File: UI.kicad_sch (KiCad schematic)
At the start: 15 parts, among them J501 EXT LEDS, SW501 SW_Push, SW502 SW_Push

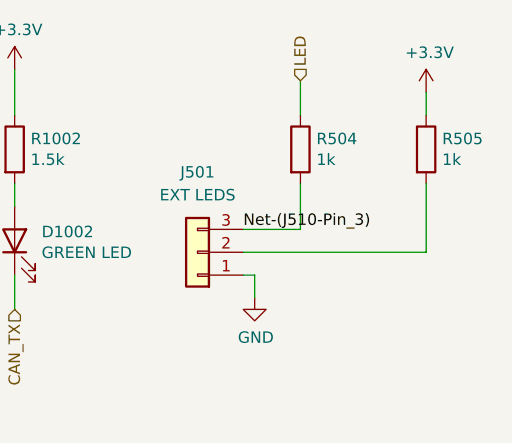
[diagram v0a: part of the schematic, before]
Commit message: Adjust external LED resistor values for ~5 mA drive current
Added series resistors for optional external panel LEDs on the GPIO13 (blue)
and 3V3 (red) indicator lines. On-board LEDs retain their existing 2 kΩ
resistors; external LEDs now use separate resistors sized for ~5 mA.

Red LED:
- Vf ≈ 2.1 V
- Vr = 3.3 V – 2.1 V = 1.2 V
- R = 1.2 V / 0.005 A = 240 Ω

Blue LED:
- Vf typically ≈ 3.0 V at a few mA (3.3 V worst case simply reduces brightness)
- Vr = 3.3 V – 3.0 V = 0.3 V
- R = 0.3 V / 0.005 A = 75 Ω

Resulting currents fall in the 3–5 mA range depending on LED tolerance, with
total GPIO13 load remaining well below ESP32-S3 limits. Red and blue LEDs now
have comparable perceived brightness.

Resistor values added:
- External red LED: 240 Ω
- External blue LED: 75 Ω
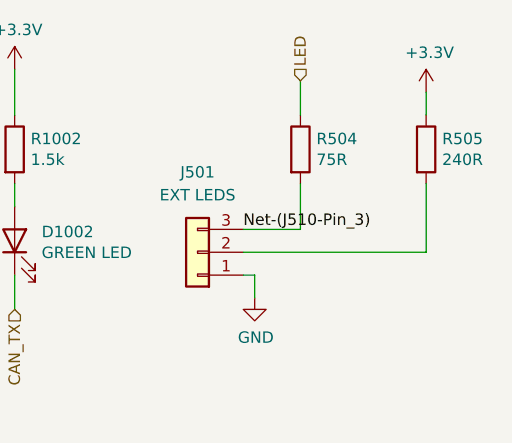
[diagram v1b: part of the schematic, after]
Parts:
- R504: value 1k -> 75R; LCSC C11702 -> C25133
- R505: value 1k -> 240R; LCSC C11702 -> C25094
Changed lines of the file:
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@@
 			)
 		)
-		(property "Value" "1k"
+		(property "Value" "75R"
 			(at 127.508 37.973 0)
 			(effects
@@
 			)
 		)
-		(property "LCSC" "C11702"
+		(property "LCSC" "C25133"
 			(at 125.73 36.83 0)
 			(effects
@@
 			)
 		)
-		(property "Value" "1k"
+		(property "Value" "240R"
 			(at 141.478 37.973 0)
 			(effects
@@
 			)
 		)
-		(property "LCSC" "C11702"
+		(property "LCSC" "C25094"
 			(at 139.7 36.83 0)
 			(effects

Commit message: Moved ESP32-S3 + larger pin headers
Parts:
- J501: footprint Connector_PinHeader_1.00mm:PinHeader_1x03_P1.00mm_Vertical -> Connector_PinHeader_2.00mm:PinHeader_1x03_P2.00mm_Vertical; LCSC C36499287 -> C49326238
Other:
- company: Hat Labs Ltd -> Fifty One North Limited
- title: Hat Labs Marine Engine & Tank interface (HALMET) -> Bluefin Marine Processor
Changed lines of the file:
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@@
 	(paper "A4")
 	(title_block
-		(title "Hat Labs Marine Engine & Tank interface (HALMET)")
-		(date "2024-01-18")
-		(rev "1.0.1")
-		(company "Hat Labs Ltd")
-		(comment 1 "https://creativecommons.org/licenses/by-sa/4.0")
-		(comment 2 "To view a copy of this license, visit ")
-		(comment 3 "HALMET is licensed under CC BY-SA 4.0.")
+		(title "Bluefin Marine Processor")
+		(date "2026-01-08")
+		(rev "1.0.0")
+		(company "Fifty One North Limited")
+		(comment 1 "https://creativecommons.org/licenses/by-sa/4.0/")
+		(comment 2 "Bluefin is licensed under CC BY-SA 4.0")
+		(comment 3 "Modifications © 2026 Fiftyone North Ltd.")
+		(comment 4 "Based on an original design by Hat Labs Ltd.")
 	)
 	(text "Reset"
@@
 			)
 		)
-		(property "Footprint" "Connector_PinHeader_1.00mm:PinHeader_1x03_P1.00mm_Vertical"
+		(property "Footprint" "Connector_PinHeader_2.00mm:PinHeader_1x03_P2.00mm_Vertical"
 			(at 114.3 48.26 0)
 			(effects
@@
 			)
 		)
-		(property "LCSC" "C36499287"
+		(property "LCSC" "C49326238"
 			(at 114.3 48.26 0)
 			(effects

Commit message: Updates LCSC part numbers.
Updates LCSC part numbers in the schematics and PCB to reflect the correct components.

This ensures accurate component sourcing and BOM generation.
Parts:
- J501: LCSC C49326238 -> C541857
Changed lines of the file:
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@@
 			)
 		)
-		(property "LCSC" "C49326238"
+		(property "LCSC" "C541857"
 			(at 114.3 48.26 0)
 			(effects
